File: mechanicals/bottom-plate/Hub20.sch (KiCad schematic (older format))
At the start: 4 parts

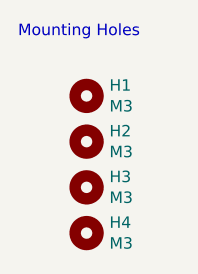
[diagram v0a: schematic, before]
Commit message: limit 2U to 3 pin only
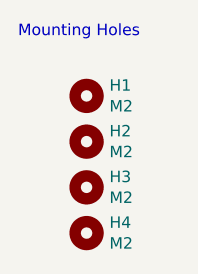
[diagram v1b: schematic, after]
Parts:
- H1, H2, H3, H4: value M3 -> M2; footprint MountingHole:MountingHole_3.2mm_M3 -> MountingHole:MountingHole_2.2mm_M2
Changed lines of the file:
@@
 P 11450 10850
 F 0 "H3" H 11550 10896 50  0000 L CNN
-F 1 "M3" H 11550 10805 50  0000 L CNN
-F 2 "MountingHole:MountingHole_3.2mm_M3" H 11450 10850 50  0001 C CNN
+F 1 "M2" H 11550 10805 50  0000 L CNN
+F 2 "MountingHole:MountingHole_2.2mm_M2" H 11450 10850 50  0001 C CNN
 F 3 "~" H 11450 10850 50  0001 C CNN
 	1    11450 10850
@@
 P 11450 11050
 F 0 "H4" H 11550 11096 50  0000 L CNN
-F 1 "M3" H 11550 11005 50  0000 L CNN
-F 2 "MountingHole:MountingHole_3.2mm_M3" H 11450 11050 50  0001 C CNN
+F 1 "M2" H 11550 11005 50  0000 L CNN
+F 2 "MountingHole:MountingHole_2.2mm_M2" H 11450 11050 50  0001 C CNN
 F 3 "~" H 11450 11050 50  0001 C CNN
 	1    11450 11050
@@
 P 11450 10450
 F 0 "H1" H 11550 10496 50  0000 L CNN
-F 1 "M3" H 11550 10405 50  0000 L CNN
-F 2 "MountingHole:MountingHole_3.2mm_M3" H 11450 10450 50  0001 C CNN
+F 1 "M2" H 11550 10405 50  0000 L CNN
+F 2 "MountingHole:MountingHole_2.2mm_M2" H 11450 10450 50  0001 C CNN
 F 3 "~" H 11450 10450 50  0001 C CNN
 	1    11450 10450
@@
 P 11450 10650
 F 0 "H2" H 11550 10696 50  0000 L CNN
-F 1 "M3" H 11550 10605 50  0000 L CNN
-F 2 "MountingHole:MountingHole_3.2mm_M3" H 11450 10650 50  0001 C CNN
+F 1 "M2" H 11550 10605 50  0000 L CNN
+F 2 "MountingHole:MountingHole_2.2mm_M2" H 11450 10650 50  0001 C CNN
 F 3 "~" H 11450 10650 50  0001 C CNN
 	1    11450 10650
